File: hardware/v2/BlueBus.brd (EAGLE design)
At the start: 95 x 65 mm, 142 parts, among them J1 3PIN_953442_1, J2 6PIN_953442_1, J3 6PIN_5_103166_1, J4 SJ2-35853A-SMT-TR, J5 SMB_CONN, J6 USB3080-30-01-A, J7 PCM12SMTR, J8 TC2030NL, Q1 NMOSFET-BSS138K, Q2 NMOSFET-BSS138K, Q3 PMOSFET-DMP32D4SSOT323, U1 MPQ4420, U10 PCM5122, U11 PAM8406, U2 TH3122.4, U3 FT231XS, U4 S-1212BC0-U5T1U, U5 XC6210, U6 CAT25M01, U7 PIC24FJ1024GA606, U8 BM83SM1, U9 DIT4096

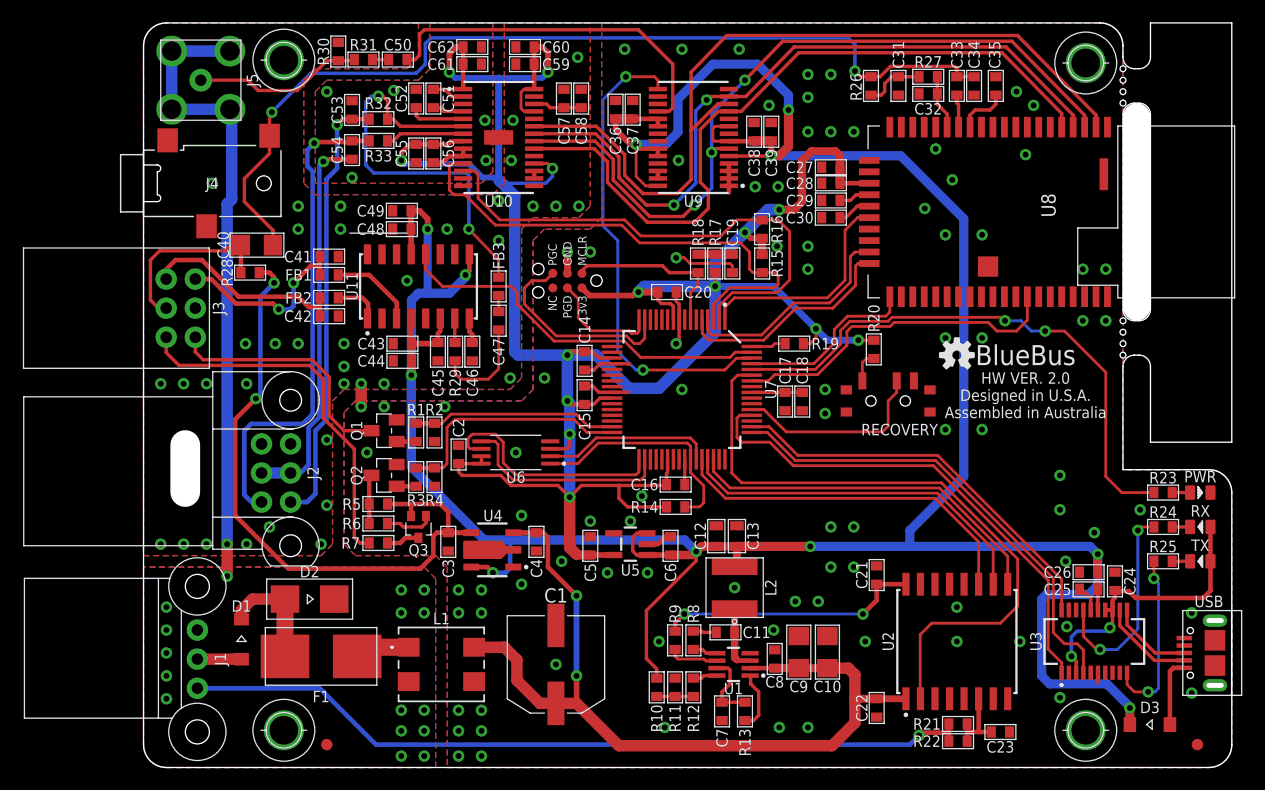
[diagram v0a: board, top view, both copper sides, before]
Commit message: [IMP] hardware: v2 Bugfixes * Swap BT UART lines * Move MCU_VER to pin 6 of PIC24 as pin 65 was used in 1.x * Swap MCLK and BCLK on DIT4096 * Add Cutout to board edge for panelization * Add diagonal fiducial
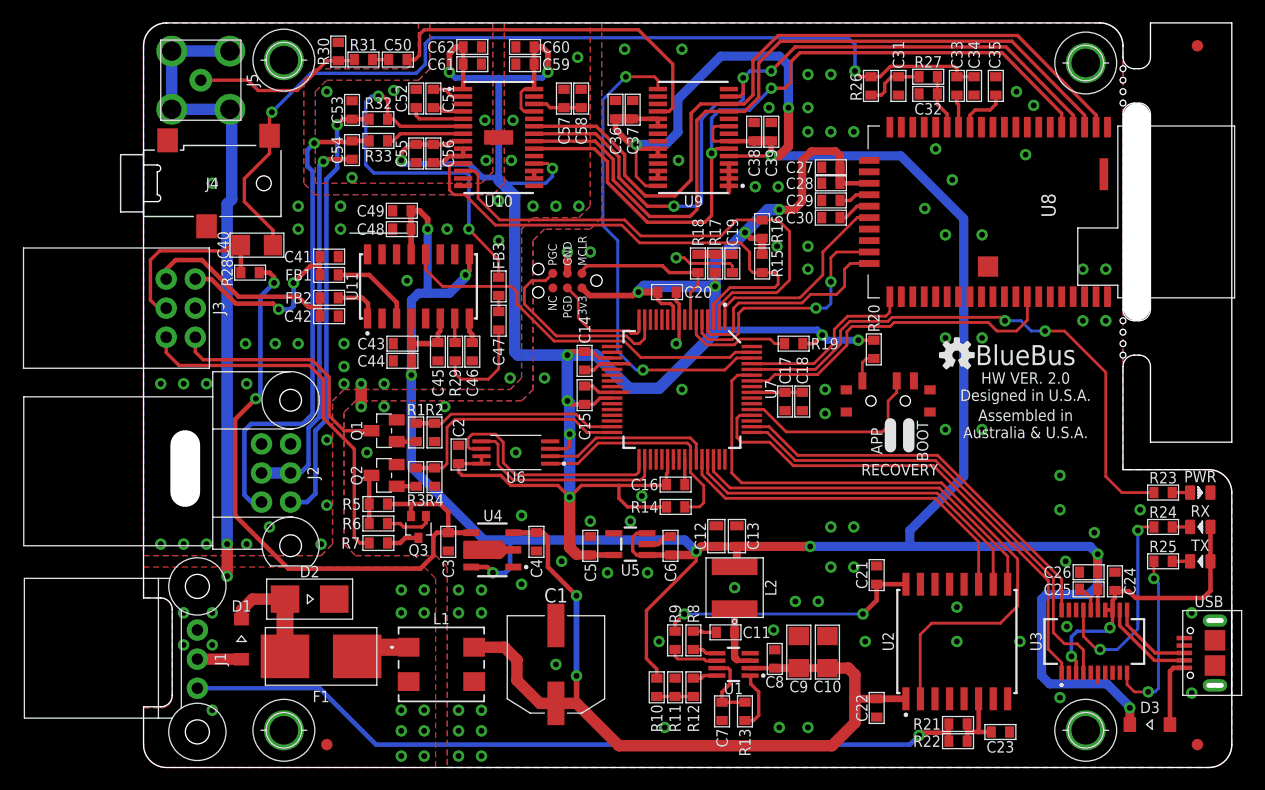
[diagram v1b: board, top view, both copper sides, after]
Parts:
- added FID3: FIDUCIAL_1MM, MF_Aesthetics:FIDUCIAL_1MM
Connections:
- removed net I2S_CLK: U10.21, U8.3, U9.6
- removed net I2S_SCK: U10.20, U8.5, U9.11
- new net I2S_BCK: U10.21, U8.3, U9.11
- new net I2S_MCLK: U10.20, U8.5, U9.6
- net BT_URX: now also U7.4; no longer U7.5
- net BT_UTX: now also U7.5; no longer U7.4
- net MCU_VER: now also U7.6; no longer U7.64
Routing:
- net I2S_BCK: track 0.00 -> 68.2 mm
- net I2S_CLK: track 67.4 -> 0.00 mm, vias 3 -> 0
- net I2S_MCLK: track 0.00 -> 67.0 mm, vias 0 -> 2
- net I2S_SCK: track 64.4 -> 0.00 mm
- net MCU_VER: track 3.00 -> 9.76 mm
- net I2S_LRCK: track 72.0 -> 67.5 mm
- net I2S_DOUT: track 63.7 -> 68.1 mm, vias 2 -> 3
- net BT_UTX: track 19.6 -> 22.5 mm, vias 0 -> 2
- net 5V: track 270.2 -> 272.3 mm
- net 3.3V: track 226.1 -> 224.5 mm
- net BT_MFB: track 19.5 -> 18.1 mm
- net GND: vias 125 -> 124
- removed copper zone on layer 16, net GND_FLT
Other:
- outline, holes or cut-outs redrawn
- board text added: "APP"
- board text added: "Assembled in Australia & U.S.A."
- board text added: "BOOT"
- board text removed: "Assembled in Australia"

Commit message: [IMP] hardware: v2 Bugfixes * Add missing ground plane for GND_FLT on bottom layer * Point all cathodes in the same directory for the three LEDs
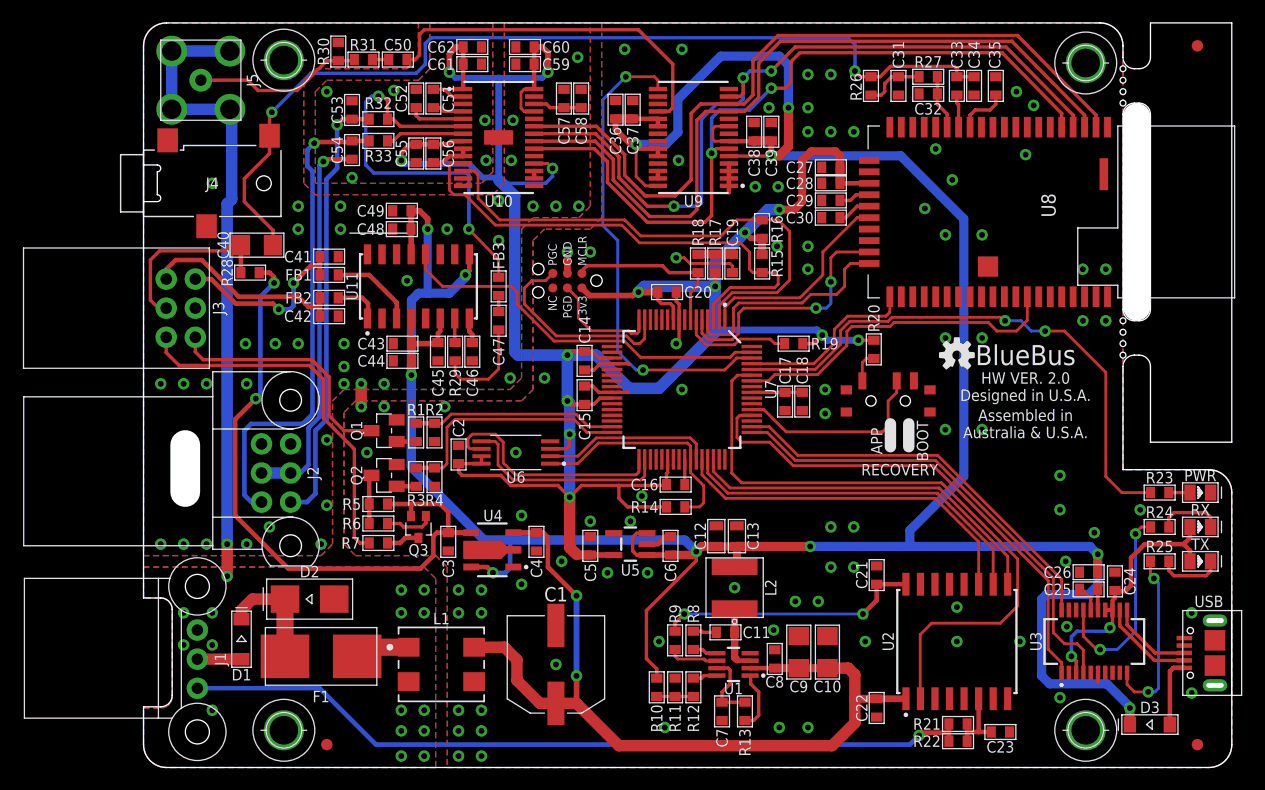
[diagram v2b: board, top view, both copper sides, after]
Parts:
- moved R23 0.30 mm to (88.7, 24.0)
- moved R24 0.30 mm to (88.7, 21.0)
- moved R25 0.30 mm to (88.7, 18.0)
- turned RX to 0 degrees
- turned TX to 0 degrees
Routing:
- net SYS_RX_LED_RES: track 1.56 -> 5.72 mm
- net SYS_TX_LED_RES: track 1.56 -> 5.66 mm
- net USB_3V3: track 25.5 -> 23.7 mm
- added copper zone on layer 16, net GND_FLT

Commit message: [IMP] hardware: v2 Bugfixes * Ensure 100nF caps are closest to pins instead of 10uF/1uF * Fix bottom silkscreen * Fix recovery slider silkscreen * Renumber passives per convention (counter-clockwise)
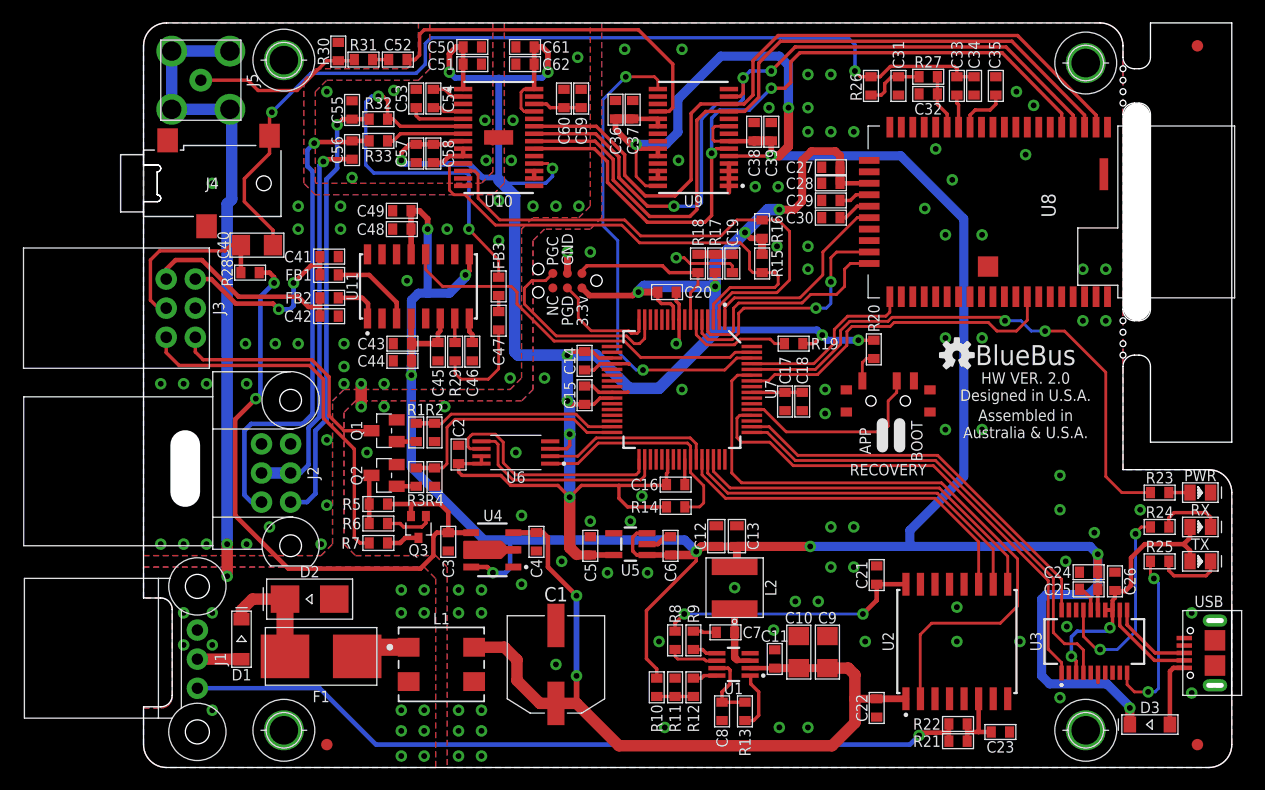
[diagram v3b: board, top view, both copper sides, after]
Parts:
- C24, C36, C50, C58, C59, C61: value 0.1uF -> 10uF
- C26, C37, C57, C60, C62: value 10uF -> 0.1uF
- C43: value 10uF -> 1uF
- C44: value 1uF -> 10uF
- C51, C52: value 2.2uF -> 0.1uF
- C53, C54: value 10nF -> 2.2uF
- C55: value 0.1uF -> 10nF
- C56: value 10uF -> 10nF
- R8: value 20 -> 100k
- R9: value 100k -> 20
- moved C57 13.8 mm to (23.8, 53.6), turned to 270 degrees
- moved C58 13.8 mm to (25.3, 53.6), turned to 270 degrees
- moved C54 8.41 mm to (25.3, 58.4)
- moved C56 7.11 mm to (18.2, 53.9)
- moved C7 6.91 mm to (50.8, 11.8), turned to 0 degrees
- moved C55 6.77 mm to (18.2, 57.4), turned to 90 degrees
- moved C50 6.59 mm to (28.7, 62.9), turned to 0 degrees
- moved C8 6.49 mm to (50.5, 4.90), turned to 270 degrees
- moved C59 5.75 mm to (38.2, 58.4), turned to 90 degrees
- moved C53 5.69 mm to (23.8, 58.4), turned to 270 degrees
- moved C60 5.64 mm to (36.7, 58.4), turned to 90 degrees
- moved C11 4.89 mm to (55.1, 9.47), turned to 90 degrees
- moved C61 4.84 mm to (33.3, 62.9), turned to 180 degrees
- moved C62 4.84 mm to (33.3, 61.4), turned to 180 degrees
- moved C51 4.53 mm to (28.7, 61.4), turned to 0 degrees
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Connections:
- net 3.3V: now also C50.1, C51.1, C57.1, C58.1; no longer C55.1, C56.1, C59.1, C60.1
- net 5V: now also C24.1; no longer C26.1
- net 5VREG_BS: now also R9.1; no longer R8.1
- net 5VREG_BS_CAP: now also C7.1, R9.2; no longer C11.1, R8.2
- net 5VREG_EN: now also R8.1; no longer R9.1
- net 5VREG_SW: now also C7.2; no longer C11.2
- net 5VREG_VCC: now also C8.1; no longer C7.1
- net AGND: now also C50.2, C51.2, C53.1, C57.2, C58.2; no longer C52.1, C53.2, C54.2, C61.2, C62.2
- net DAC_CAPM: now also C54.2; no longer C51.2
- net DAC_CAPP: now also C54.1; no longer C51.1
- net DAC_LDOO: now also C59.1, C60.1; no longer C57.1, C58.1
- net DAC_VNEG: now also C53.2; no longer C52.2
- net GND: now also C11.2, C61.2, C62.2; no longer C57.2, C58.2, C7.2
- net IBUS_5V: now also R8.2; no longer R9.2
- net SPDIF_TX_FLT: now also C52.1; no longer C50.1
- net SPDIF_TX_RES: now also C52.2; no longer C50.2
- net SPKR_OUT_L: now also C55.1; no longer C53.1
- net SPKR_OUT_R: now also C56.1; no longer C54.1
- net USB_3V3: now also C26.1; no longer C24.1
- net VIN: now also C11.1; no longer C8.1
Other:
- outline, holes or cut-outs redrawn
- board text added: "3.3v"
- board text removed: "3v3"
